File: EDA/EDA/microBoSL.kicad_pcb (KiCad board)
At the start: 2 copper layers, 79 x 69.8 mm, 67 parts, among them CON1 Micro_SD_Card, CON2 BARREL_JACK, IC2 SIM7000, J1 Screw_Terminal_1x06, J10 Conn_01x08, J2 Screw_Terminal_1x04, J3 Screw_Terminal_1x02, J4 Screw_Terminal_1x08, J5 Screw_Terminal_1x04, J6 RJ45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

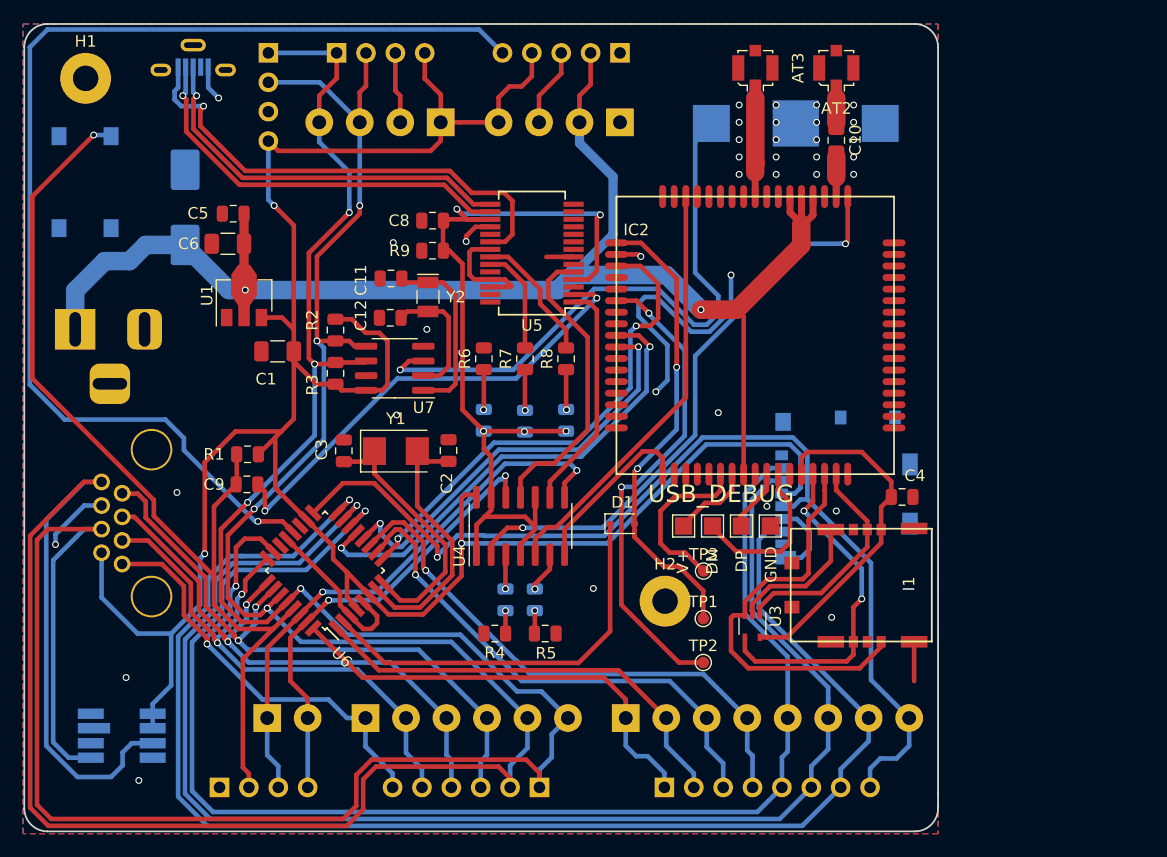
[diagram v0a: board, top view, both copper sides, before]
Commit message: added new footprints
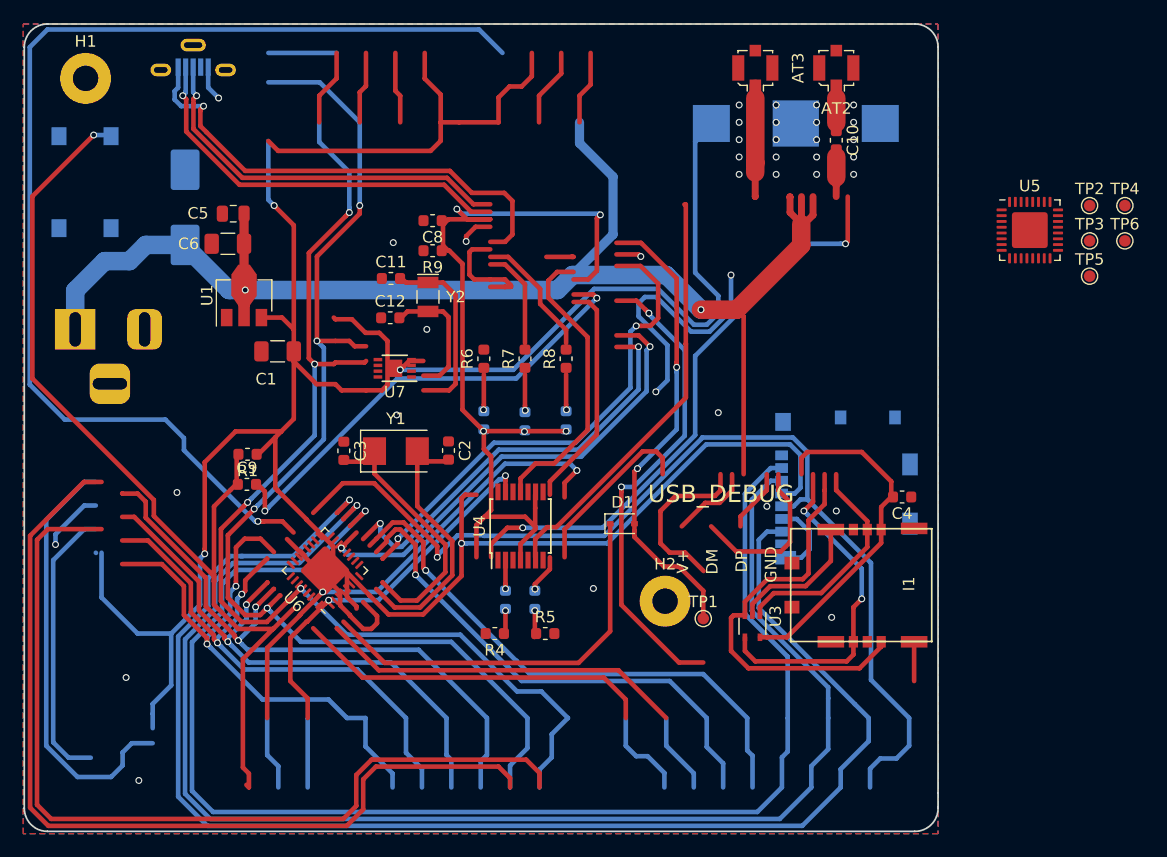
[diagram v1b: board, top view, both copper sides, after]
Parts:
- removed IC2: SIM7000, SIMFootprints:SIM7000
- removed J1: Screw_Terminal_1x06, TerminalBlock_Phoenix:TerminalBlock_Phoenix_PT-1,5-6-3.5-H_1x06_P3.50mm_Horizontal
- removed J10: Conn_01x08, Connector_PinHeader_2.54mm:PinHeader_1x08_P2.54mm_Vertical
- removed J2, J5: Screw_Terminal_1x04, TerminalBlock_Phoenix:TerminalBlock_Phoenix_PT-1,5-4-3.5-H_1x04_P3.50mm_Horizontal
- removed J3: Screw_Terminal_1x02, TerminalBlock_Phoenix:TerminalBlock_Phoenix_PT-1,5-2-3.5-H_1x02_P3.50mm_Horizontal
- removed J4: Screw_Terminal_1x08, TerminalBlock_Phoenix:TerminalBlock_Phoenix_PT-1,5-8-3.5-H_1x08_P3.50mm_Horizontal
- removed J6: RJ45, SIMFootprints:RJ_45
- removed J8: Conn_01x05, Connector_PinHeader_2.54mm:PinHeader_1x05_P2.54mm_Vertical
- removed J9: Conn_01x06, Connector_PinHeader_2.54mm:PinHeader_1x06_P2.54mm_Vertical
- removed P2, P3, P4: CONN_01X04, Connector_PinHeader_2.54mm:PinHeader_1x04_P2.54mm_Vertical
- removed R2, R3: 10 kΩ, Resistor_SMD:R_0805_2012Metric
- removed TP7: TestPoint, TestPoint:TestPoint_Pad_1.5x1.5mm
- removed U2: MS5803, SIMFootprints:MS5803
- C10, C11, C12, C2, C3, C4, C8, C9: footprint Capacitor_SMD:C_0805_2012Metric -> Capacitor_SMD:C_0603_1608Metric
- D2, D3, D4, D5, D6: footprint LED_SMD:LED_0805_2012Metric -> LED_SMD:LED_0603_1608Metric
- G1: value LOGO -> BoSL_Graphic
- R1, R4, R5, R6, R7, R8, R9: footprint Resistor_SMD:R_0805_2012Metric -> Resistor_SMD:R_0603_1608Metric
- TP4, TP5, TP6: value TestPoint -> TEST; footprint TestPoint:TestPoint_Pad_1.5x1.5mm -> TestPoint:TestPoint_Pad_D1.0mm
- U4: footprint Package_SO:SOIC-14_3.9x8.7mm_P1.27mm -> Package_SO:TSSOP-14_4.4x5mm_P0.65mm
- U5: value FT232RL -> FT232RQ; footprint Package_SO:SSOP-28_5.3x10.2mm_P0.65mm -> Package_DFN_QFN:QFN-32-1EP_5x5mm_P0.5mm_EP3.1x3.1mm
- U6: footprint Package_QFP:TQFP-32_7x7mm_P0.8mm -> Package_DFN_QFN:QFN-32-1EP_5x5mm_P0.5mm_EP3.1x3.1mm
- U7: footprint Package_SO:SOIC-8_3.9x4.9mm_P1.27mm -> Package_DFN_QFN:DFN-8-1EP_3x2mm_P0.5mm_EP1.3x1.5mm
- moved TP2 51.7 mm to (205.6, 78.7)
- moved TP4 47.1 mm to (208.7, 78.7)
- moved TP3 43.9 mm to (205.6, 81.8)
- moved U5 43.1 mm to (200.4, 80.8), turned to 0 degrees
- moved TP6 41.3 mm to (208.7, 81.8)
- moved TP5 39.1 mm to (205.6, 84.8)
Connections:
- C8 pad 1: TTL_3.3V -> GND
- C8 pad 2: GND -> TTL_3.3V
- J7 pad 6: (no net) -> Net-(J7-Pad6)
- TP2 pad 1: Net-(IC2-Pad6) -> V_1.8
- TP4 pad 1: /USB_VBUS -> Net-(TP4-Pad1)
- TP5 pad 1: /DM -> Net-(TP5-Pad1)
- TP6 pad 1: /DP -> Net-(TP6-Pad1)
- U3 pad 1: Net-(I1-Pad2) -> Net-(I1-Pad3)
- U3 pad 3: Net-(I1-Pad3) -> Net-(I1-Pad6)
- U3 pad 4: Net-(I1-Pad6) -> Net-(I1-Pad2)
- U5 pad 1: AND_RX -> TTL_3.3V
- U5 pad 12: Net-(U5-Pad12) -> (no net)
- U5 pad 13: Net-(U5-Pad13) -> (no net)
- U5 pad 14: Net-(U5-Pad14) -> USB_DP
- U5 pad 15: USB_DP -> USB_DM
- U5 pad 16: USB_DM -> TTL_3.3V
- U5 pad 17: TTL_3.3V -> GND
- U5 pad 18: GND -> Net-(U5-Pad18)
- U5 pad 19: Net-(U5-Pad19) -> USB_V
- U5 pad 2: Net-(C9-Pad2) -> AND_TX
- U5 pad 20: USB_V -> GND
- U5 pad 21: GND -> Net-(R8-Pad2)
- U5 pad 22: Net-(R8-Pad2) -> Net-(R7-Pad2)
- U5 pad 23: Net-(R7-Pad2) -> (no net)
- U5 pad 24: Net-(U5-Pad24) -> GND
- U5 pad 25: GND -> (no net)
- U5 pad 26: GND -> Net-(U5-Pad26)
- U5 pad 4: TTL_3.3V -> GND
- U5 pad 5: AND_TX -> (no net)
- U5 pad 7: GND -> Net-(U5-Pad7)
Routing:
- net PWR_STAT: track 36.5 -> 0.00 mm
- net Net-(D3-Pad2): track 3.29 -> 39.8 mm
- net TTL_3.3V: track 76.5 -> 110.1 mm, vias 5 -> 7
- net TLL_TX: track 39.6 -> 6.00 mm, vias 2 -> 0
- net Net-(TP3-Pad1): track 14.8 -> 0.00 mm
- net Net-(IC2-Pad23): track 0.00 -> 14.8 mm
